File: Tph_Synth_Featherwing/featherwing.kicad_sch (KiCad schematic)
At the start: 1 part

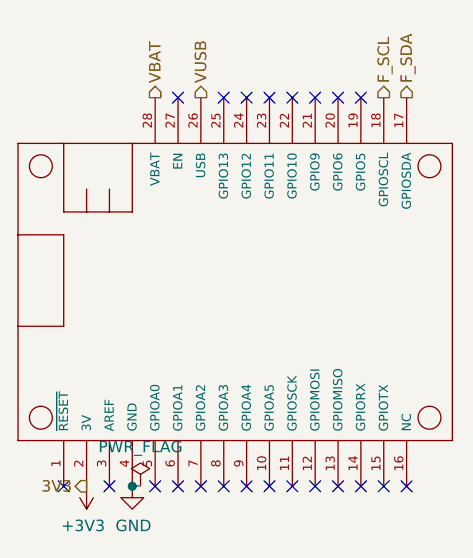
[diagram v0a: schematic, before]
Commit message: Upgrade design to KiCad 10; clear ERC and DRC violations
Co-authored-by: Copilot <223556219+Copilot@users.noreply.github.com>
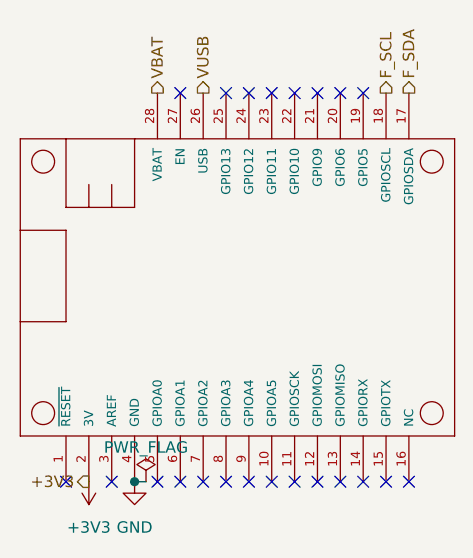
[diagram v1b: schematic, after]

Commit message: Release v0.4 with complete KiCad 10 schematic-PCB parity
Synchronize pad nets, schematic paths, component fields and BOM exclusions while retaining routing and placement. Restore project-local STEP models, fix edge silkscreen using local footprint variants, update revision metadata and improve schematic readability. Include inspected PDF and PCB renders.

Co-authored-by: Copilot <223556219+Copilot@users.noreply.github.com>
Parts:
- MS1: footprint featherwing:adafruit_featherwing -> FeatherWing_v04:adafruit_featherwing_HostOutlineOnFab
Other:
- title: (none) -> 3-Phase Synth FeatherWing
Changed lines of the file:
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@@
 	(generator_version "10.0")
 	(paper "A4")
+	(title_block
+		(title "3-Phase Synth FeatherWing")
+		(date "2026-10-28")
+		(rev "0.4")
+	)
 	(junction
 		(at 134.62 90.17)
@@
 		(dnp no)
 		(property "Reference" "MS1"
-			(at 121.92 85.09 0)
-			(hide yes)
+			(at 146.05 67.31 0)
+			(hide no)
 			(show_name no)
 			(do_not_autoplace no)
@@
 		)
 		(property "Value" "ADAFRUIT_FEATHERWING"
-			(at 121.92 85.09 0)
-			(hide yes)
+			(at 146.05 69.85 0)
+			(hide no)
 			(show_name no)
 			(do_not_autoplace no)
@@
 			)
 		)
-		(property "Footprint" "featherwing:adafruit_featherwing"
+		(property "Footprint" "FeatherWing_v04:adafruit_featherwing_HostOutlineOnFab"
 			(at 121.92 85.09 0)
 			(hide yes)
@@
 				)
 			)
+			(hide yes)
 		)
 		(property "Footprint" ""
